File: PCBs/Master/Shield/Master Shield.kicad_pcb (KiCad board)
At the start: 2 copper layers, 78.8 x 53.3 mm, 32 parts, among them J1 Power, J2 PWM, J3 Communication

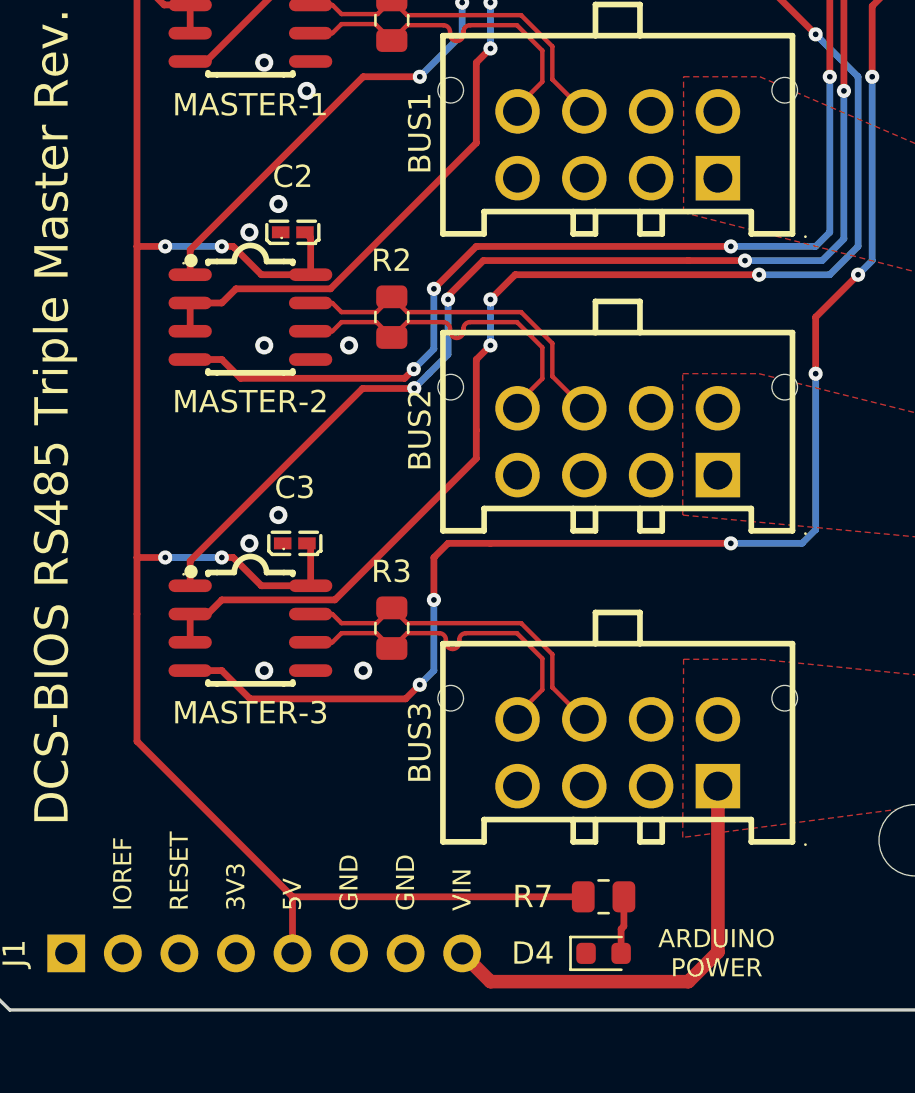
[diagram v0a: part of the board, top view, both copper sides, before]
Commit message: Updated micro-fit pinout for more power
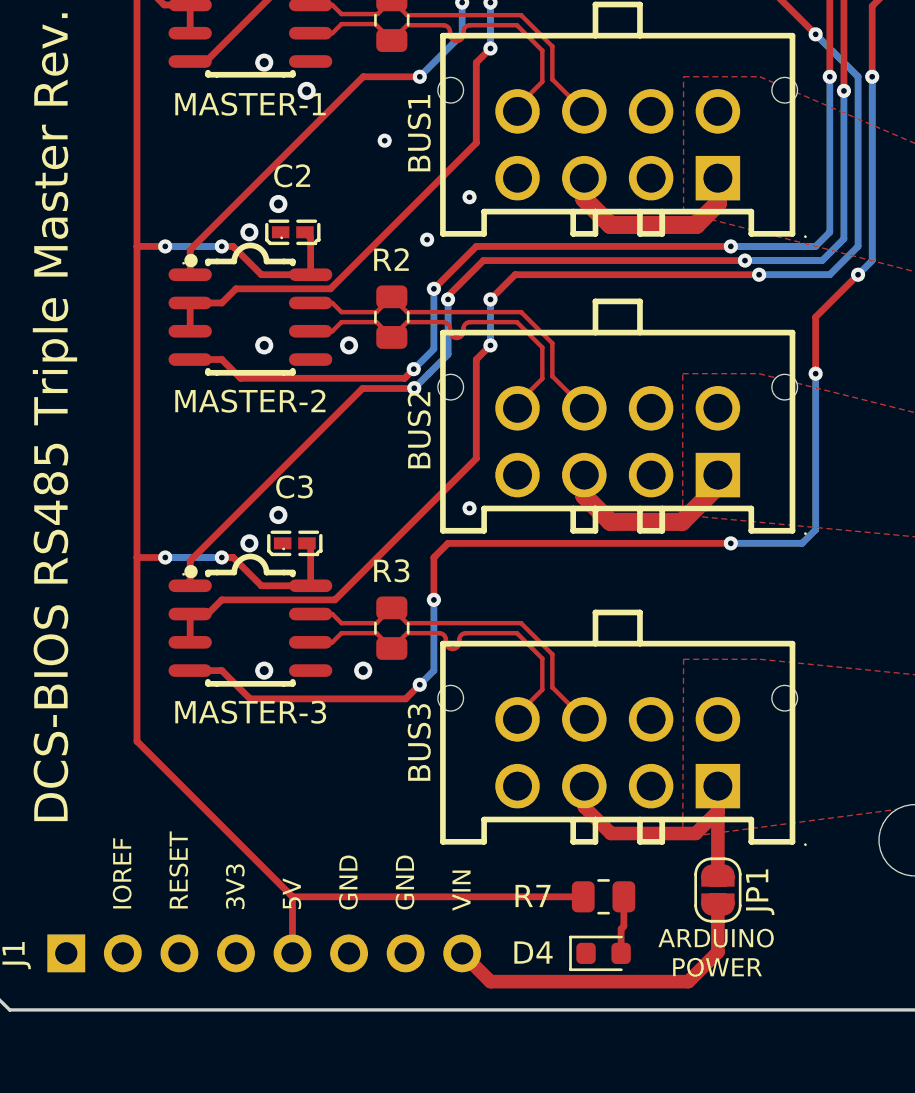
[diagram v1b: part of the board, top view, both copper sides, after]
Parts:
- added JP1: SolderJumper_2_Open, Jumper:SolderJumper-2_P1.3mm_Open_RoundedPad1.0x1.5mm, F.Cu at (157.2, 94.6)
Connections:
- BUS1 pad 3: unconnected-(BUS1-Pad3) -> /12V_Fused
- BUS1 pad 4: unconnected-(BUS1-Pad4) -> GND
- BUS2 pad 3: unconnected-(BUS2-Pad3) -> /12V_2_Fused
- BUS2 pad 4: unconnected-(BUS2-Pad4) -> GND
- BUS3 pad 3: unconnected-(BUS3-Pad3) -> 12V_3_Fused
- BUS3 pad 4: unconnected-(BUS3-Pad4) -> GND
- J1 pad 8: 12V_3_Fused -> Net-(J1-Pad8)
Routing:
- net Net-(J1-Pad8): track 0.00 -> 14.7 mm
- net /12V_Fused: track 5.96 -> 14.9 mm
- net /12V_2_Fused: track 5.96 -> 14.5 mm
- net 12V_3_Fused: track 26.0 -> 17.8 mm
- net GND: vias 12 -> 16
